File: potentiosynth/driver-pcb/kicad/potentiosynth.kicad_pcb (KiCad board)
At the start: 2 copper layers, 127 x 63.5 mm, 89 parts, among them J1 Conn_01x40, U0 L7815, U1 LM358, U2 LM358, U3 LM358, U4 LM358, U5 LM358, U6 LM358, U7 LM358, U8 LM358

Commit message: first draft driver-pcb
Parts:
- removed QD1, QD2, QD3, QD4, QD5, QD6, QD7, QD8: IRF630, Package_TO_SOT_THT:TO-220-3_Vertical
- removed R0: 10k, Resistor_SMD:R_1206_3216Metric
- removed R1: 68, Resistor_SMD:R_1206_3216Metric
- removed RL1, RL2, RL3, RL4, RL5, RL6, RL7, RL8: 10, Resistor_SMD:R_1206_3216Metric
- removed RV0: 1k, Potentiometer_THT:Potentiometer_Bourns_3296X_Horizontal
- removed TP3: TestPoint, TestPoint:TestPoint_THTPad_D3.0mm_Drill1.5mm
- QE1, QE2, QE3, QE4, QE5, QE6, QE7, QE8: value 2N7000 -> Q_NMOS_GSD; footprint Package_TO_SOT_THT:TO-92_Inline -> Package_TO_SOT_SMD:SOT-23_Handsoldering
- RV1, RV2, RV3, RV4, RV5, RV6, RV7, RV8: value 2k -> R_POT_US
- U0: value L7815 -> R-7815-0.5; footprint Package_TO_SOT_THT:TO-220-3_Vertical -> footprints:CONV_VXO7815-500-M
- U1, U2, U3, U4, U5, U6, U7, U8: value LM358 -> TLV9152IDR; footprint Package_DIP:DIP-8_W7.62mm_LongPads -> Package_SO:SOIC-8_3.9x4.9mm_P1.27mm
- moved TP1 20.3 mm to (158.8, 67.9)
- moved TP2 20.3 mm to (165.1, 67.9)
- moved U2 13.3 mm to (82.5, 99.1)
- moved U3 13.3 mm to (95.2, 99.1)
- moved U4 13.3 mm to (108.0, 99.1)
- moved U5 13.3 mm to (120.7, 99.1)
- moved U6 13.3 mm to (133.3, 99.1)
- moved U7 13.3 mm to (146.1, 99.1)
- moved U8 13.3 mm to (158.8, 99.1)
- moved U1 13.3 mm to (69.8, 99.1)
- moved C3 12.7 mm to (142.2, 71.1)
- moved RF1 10.2 mm to (68.5, 90.2), turned to 180 degrees
- moved RF3 10.1 mm to (93.8, 90.2), turned to 180 degrees
- moved RF2 10.1 mm to (81.2, 90.2), turned to 180 degrees
- moved RF4 10.1 mm to (106.5, 90.2), turned to 180 degrees
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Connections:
- J1 pad 1: /1/RETURN -> /1/REFERENCE
- J1 pad 10: /2/SUPPLY -> /2/COUNTER
- J1 pad 11: /3/RETURN -> /3/REFERENCE
- J1 pad 15: /3/SUPPLY -> /3/COUNTER
- J1 pad 16: /4/RETURN -> /4/REFERENCE
- J1 pad 20: /4/SUPPLY -> /4/COUNTER
- J1 pad 21: /5/RETURN -> /5/REFERENCE
- J1 pad 25: /5/SUPPLY -> /5/COUNTER
- J1 pad 26: /6/RETURN -> /6/REFERENCE
- J1 pad 30: /6/SUPPLY -> /6/COUNTER
- J1 pad 31: /7/RETURN -> /7/REFERENCE
- J1 pad 35: /7/SUPPLY -> /7/COUNTER
- J1 pad 36: /8/RETURN -> /8/REFERENCE
- J1 pad 40: /8/SUPPLY -> /8/COUNTER
- J1 pad 5: /1/SUPPLY -> /1/COUNTER
- J1 pad 6: /2/RETURN -> /2/REFERENCE
- QE1 pad 1: GND -> Net-(QE1-Pad1)
- QE1 pad 2: Net-(QE1-Pad2) -> GND
- QE2 pad 1: GND -> Net-(QE2-Pad1)
- QE2 pad 2: Net-(QE2-Pad2) -> GND
- QE3 pad 1: GND -> Net-(QE3-Pad1)
- QE3 pad 2: Net-(QE3-Pad2) -> GND
- QE4 pad 1: GND -> Net-(QE4-Pad1)
- QE4 pad 2: Net-(QE4-Pad2) -> GND
- QE5 pad 1: GND -> Net-(QE5-Pad1)
- QE5 pad 2: Net-(QE5-Pad2) -> GND
- QE6 pad 1: GND -> Net-(QE6-Pad1)
- QE6 pad 2: Net-(QE6-Pad2) -> GND
- QE7 pad 1: GND -> Net-(QE7-Pad1)
- QE7 pad 2: Net-(QE7-Pad2) -> GND
- QE8 pad 1: GND -> Net-(QE8-Pad1)
- QE8 pad 2: Net-(QE8-Pad2) -> GND
- R+1 pad 1: /1/CONTROL -> Net-(R+1-Pad1)
- R+2 pad 1: /1/CONTROL -> Net-(R+2-Pad1)
- R+3 pad 1: /1/CONTROL -> Net-(R+3-Pad1)
- R+4 pad 1: /1/CONTROL -> Net-(R+4-Pad1)
- R+5 pad 1: /1/CONTROL -> Net-(R+5-Pad1)
- R+6 pad 1: /1/CONTROL -> Net-(R+6-Pad1)
- R+7 pad 1: /1/CONTROL -> Net-(R+7-Pad1)
- R+8 pad 1: /1/CONTROL -> Net-(R+8-Pad1)
- R-1 pad 2: /1/RETURN -> /1/REFERENCE
- R-2 pad 2: /2/RETURN -> /2/REFERENCE
- R-3 pad 2: /3/RETURN -> /3/REFERENCE
- R-4 pad 2: /4/RETURN -> /4/REFERENCE
- R-5 pad 2: /5/RETURN -> /5/REFERENCE
- R-6 pad 2: /6/RETURN -> /6/REFERENCE
- R-7 pad 2: /7/RETURN -> /7/REFERENCE
- R-8 pad 2: /8/RETURN -> /8/REFERENCE
- RF1 pad 2: Net-(QE1-Pad2) -> Net-(QE1-Pad1)
- RF2 pad 2: Net-(QE2-Pad2) -> Net-(QE2-Pad1)
- RF3 pad 2: Net-(QE3-Pad2) -> Net-(QE3-Pad1)
- RF4 pad 2: Net-(QE4-Pad2) -> Net-(QE4-Pad1)
- RF5 pad 2: Net-(QE5-Pad2) -> Net-(QE5-Pad1)
- RF6 pad 2: Net-(QE6-Pad2) -> Net-(QE6-Pad1)
- RF7 pad 2: Net-(QE7-Pad2) -> Net-(QE7-Pad1)
- RF8 pad 2: Net-(QE8-Pad2) -> Net-(QE8-Pad1)
- RV1 pad 1: Net-(RL1-Pad2) -> +15V
- RV1 pad 2: /1/RETURN -> Net-(R+1-Pad1)
- RV1 pad 3: /1/RETURN -> GND
- RV2 pad 1: Net-(RL2-Pad2) -> +15V
- RV2 pad 2: /2/RETURN -> Net-(R+2-Pad1)
- RV2 pad 3: /2/RETURN -> GND
- RV3 pad 1: Net-(RL3-Pad2) -> +15V
- RV3 pad 2: /3/RETURN -> Net-(R+3-Pad1)
- RV3 pad 3: /3/RETURN -> GND
- RV4 pad 1: Net-(RL4-Pad2) -> +15V
- RV4 pad 2: /4/RETURN -> Net-(R+4-Pad1)
- RV4 pad 3: /4/RETURN -> GND
- RV5 pad 1: Net-(RL5-Pad2) -> +15V
- RV5 pad 2: /5/RETURN -> Net-(R+5-Pad1)
- RV5 pad 3: /5/RETURN -> GND
- RV6 pad 1: Net-(RL6-Pad2) -> +15V
- RV6 pad 2: /6/RETURN -> Net-(R+6-Pad1)
- RV6 pad 3: /6/RETURN -> GND
- RV7 pad 1: Net-(RL7-Pad2) -> +15V
- RV7 pad 2: /7/RETURN -> Net-(R+7-Pad1)
- RV7 pad 3: /7/RETURN -> GND
- RV8 pad 1: Net-(RL8-Pad2) -> +15V
- RV8 pad 2: /8/RETURN -> Net-(R+8-Pad1)
- RV8 pad 3: /8/RETURN -> GND
- U1 pad 1: Net-(QE1-Pad2) -> Net-(QE1-Pad1)
- U1 pad 5: /1/CONTROL -> Net-(R+1-Pad1)
- U1 pad 6: /1/RETURN -> /1/REFERENCE
- U1 pad 7: Net-(QD1-Pad1) -> /1/COUNTER
- U2 pad 1: Net-(QE2-Pad2) -> Net-(QE2-Pad1)
- U2 pad 5: /1/CONTROL -> Net-(R+2-Pad1)
- U2 pad 6: /2/RETURN -> /2/REFERENCE
- U2 pad 7: Net-(QD2-Pad1) -> /2/COUNTER
- U3 pad 1: Net-(QE3-Pad2) -> Net-(QE3-Pad1)
- U3 pad 5: /1/CONTROL -> Net-(R+3-Pad1)
- U3 pad 6: /3/RETURN -> /3/REFERENCE
- U3 pad 7: Net-(QD3-Pad1) -> /3/COUNTER
- U4 pad 1: Net-(QE4-Pad2) -> Net-(QE4-Pad1)
- U4 pad 5: /1/CONTROL -> Net-(R+4-Pad1)
- U4 pad 6: /4/RETURN -> /4/REFERENCE
- U4 pad 7: Net-(QD4-Pad1) -> /4/COUNTER
- U5 pad 1: Net-(QE5-Pad2) -> Net-(QE5-Pad1)
- U5 pad 5: /1/CONTROL -> Net-(R+5-Pad1)
- U5 pad 6: /5/RETURN -> /5/REFERENCE
- U5 pad 7: Net-(QD5-Pad1) -> /5/COUNTER
- U6 pad 1: Net-(QE6-Pad2) -> Net-(QE6-Pad1)
- U6 pad 5: /1/CONTROL -> Net-(R+6-Pad1)
- U6 pad 6: /6/RETURN -> /6/REFERENCE
- U6 pad 7: Net-(QD6-Pad1) -> /6/COUNTER
- U7 pad 1: Net-(QE7-Pad2) -> Net-(QE7-Pad1)
- U7 pad 5: /1/CONTROL -> Net-(R+7-Pad1)
- U7 pad 6: /7/RETURN -> /7/REFERENCE
- U7 pad 7: Net-(QD7-Pad1) -> /7/COUNTER
- U8 pad 1: Net-(QE8-Pad2) -> Net-(QE8-Pad1)
- U8 pad 5: /1/CONTROL -> Net-(R+8-Pad1)
- U8 pad 6: /8/RETURN -> /8/REFERENCE
- U8 pad 7: Net-(QD8-Pad1) -> /8/COUNTER
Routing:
- net +15V: track 556.7 -> 209.4 mm, vias 1 -> 8
- net /1/CONTROL: track 283.7 -> 0.00 mm, vias 16 -> 0
- net /2/REFERENCE: track 0.00 -> 40.2 mm
- net /8/REFERENCE: track 0.00 -> 39.9 mm
- net /4/REFERENCE: track 0.00 -> 39.9 mm
- net /3/REFERENCE: track 0.00 -> 39.9 mm
- net /5/REFERENCE: track 0.00 -> 39.9 mm
- net /7/REFERENCE: track 0.00 -> 39.7 mm
- net /1/REFERENCE: track 0.00 -> 39.7 mm
- net /6/REFERENCE: track 0.00 -> 39.7 mm
- net /7/RETURN: track 39.2 -> 0.00 mm, vias 1 -> 0
- net /6/RETURN: track 39.2 -> 0.00 mm, vias 1 -> 0
- net /5/RETURN: track 39.2 -> 0.00 mm, vias 1 -> 0
- net /4/RETURN: track 38.4 -> 0.00 mm, vias 1 -> 0
- net /3/RETURN: track 38.4 -> 0.00 mm, vias 1 -> 0
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- added copper zone on B.Cu, net +15V
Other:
- net class Default: clearance 0.2 -> 0.127
- rule trace_clearance: 0.2 -> 0.127
- board text added: "18 to 30 V"
- board text added: "BLAISE THOMPSON UW-MADISON DEPARTMENT OF CHEMISTRY WICKENS GROUP"
- board text added: "POTENTIOSYNTH REVISION A MAY 2021"
- board text removed: "BLAISE THOMPSON UW-MADISON DEPARTMENT OF CHEMISTRY INSTRUMENT SHOP"
- board text removed: "REVISION 4.1.1 MARCH 2020"
- board text removed: "≥ 18 V CENTER POSITIVE"

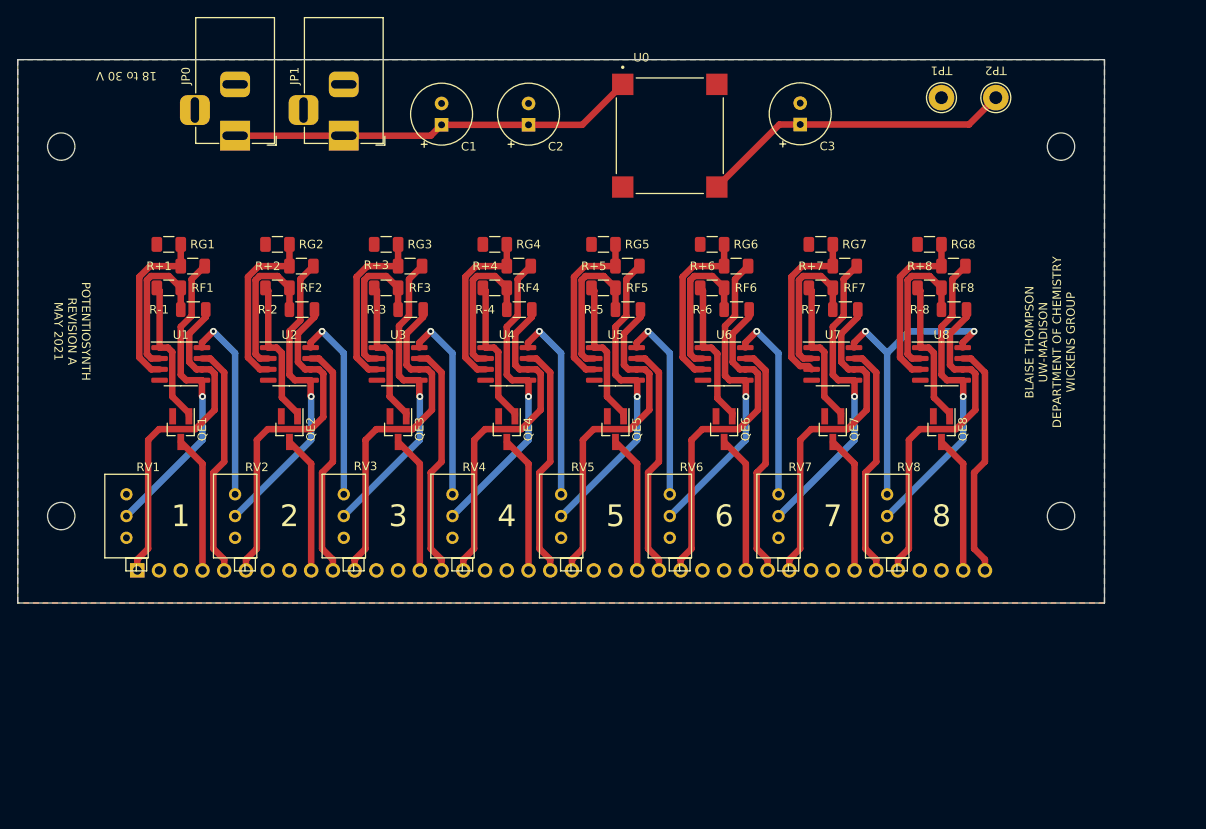
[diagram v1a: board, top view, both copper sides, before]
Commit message: added buffer amplifier
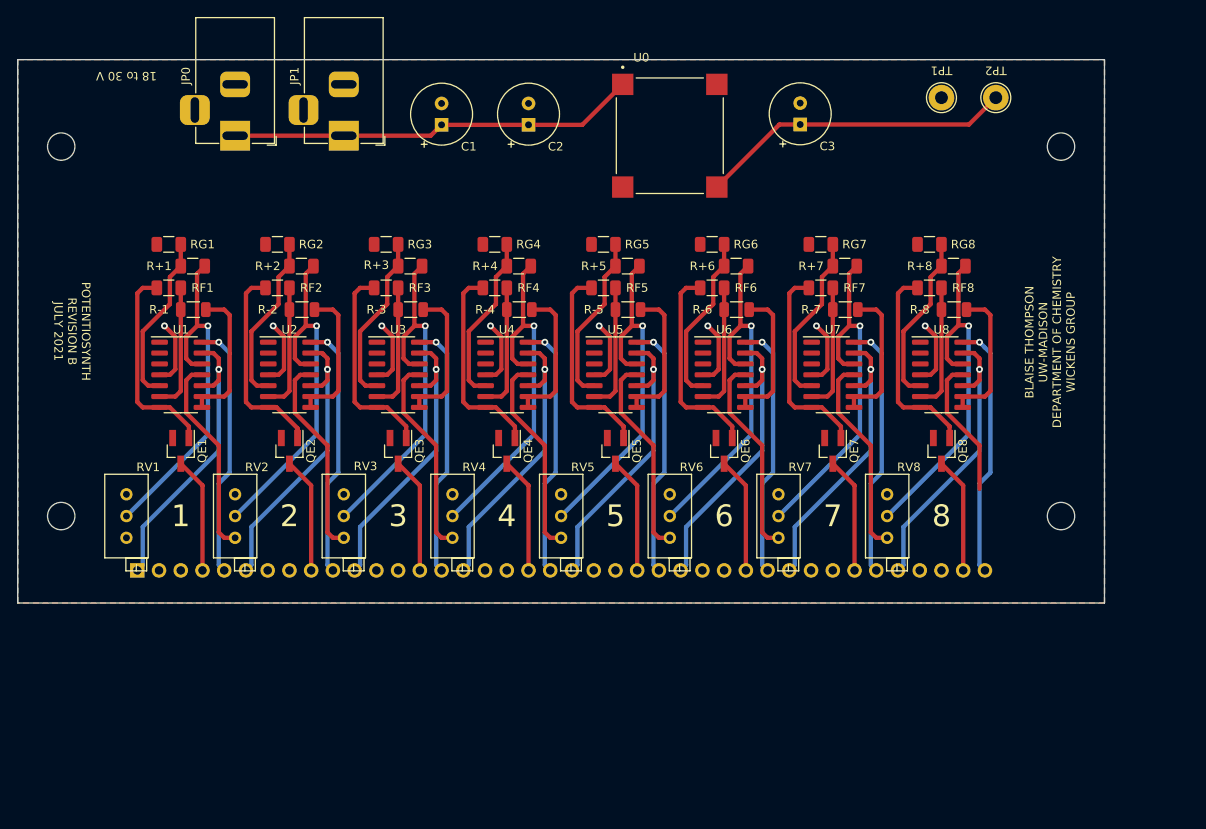
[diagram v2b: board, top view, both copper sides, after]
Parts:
- QE1, QE2, QE3, QE4, QE5, QE6, QE7, QE8: value Q_NMOS_GSD -> 2N70002K
- U1, U2, U3, U4, U5, U6, U7, U8: value TLV9152IDR -> TLV9154IDR; footprint Package_SO:SOIC-8_3.9x4.9mm_P1.27mm -> Package_SO:SOIC-14_3.9x8.7mm_P1.27mm
- moved QE1 2.54 mm to (69.8, 109.2)
- moved QE2 2.54 mm to (82.5, 109.2)
- moved QE3 2.54 mm to (95.2, 109.2)
- moved QE4 2.54 mm to (108.0, 109.2)
- moved QE5 2.54 mm to (120.7, 109.2)
- moved QE6 2.54 mm to (133.3, 109.2)
- moved QE7 2.54 mm to (146.1, 109.2)
- moved QE8 2.54 mm to (158.8, 109.2)
- moved U1 1.27 mm to (69.8, 100.3)
- moved U2 1.27 mm to (82.5, 100.3)
- moved U3 1.27 mm to (95.2, 100.3)
- moved U4 1.27 mm to (108.0, 100.3)
- moved U5 1.27 mm to (120.7, 100.3)
- moved U6 1.27 mm to (133.3, 100.3)
- moved U7 1.27 mm to (146.1, 100.3)
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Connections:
- R-1 pad 2: /1/REFERENCE -> Net-(R-1-Pad2)
- R-2 pad 2: /2/REFERENCE -> Net-(R-2-Pad2)
- R-3 pad 2: /3/REFERENCE -> Net-(R-3-Pad2)
- R-4 pad 2: /4/REFERENCE -> Net-(R-4-Pad2)
- R-5 pad 2: /5/REFERENCE -> Net-(R-5-Pad2)
- R-6 pad 2: /6/REFERENCE -> Net-(R-6-Pad2)
- R-7 pad 2: /7/REFERENCE -> Net-(R-7-Pad2)
- R-8 pad 2: /8/REFERENCE -> Net-(R-8-Pad2)
- U1 pad 1: Net-(QE1-Pad1) -> (no net)
- U1 pad 2: Net-(R-1-Pad1) -> (no net)
- U1 pad 3: Net-(R+1-Pad2) -> (no net)
- U1 pad 4: GND -> +15V
- U1 pad 5: Net-(R+1-Pad1) -> Net-(R+1-Pad2)
- U1 pad 6: /1/REFERENCE -> Net-(R-1-Pad1)
- U1 pad 7: /1/COUNTER -> Net-(QE1-Pad1)
- U1 pad 8: +15V -> Net-(R-1-Pad2)
- U2 pad 1: Net-(QE2-Pad1) -> (no net)
- U2 pad 2: Net-(R-2-Pad1) -> (no net)
- U2 pad 3: Net-(R+2-Pad2) -> (no net)
- U2 pad 4: GND -> +15V
- U2 pad 5: Net-(R+2-Pad1) -> Net-(R+2-Pad2)
- U2 pad 6: /2/REFERENCE -> Net-(R-2-Pad1)
- U2 pad 7: /2/COUNTER -> Net-(QE2-Pad1)
- U2 pad 8: +15V -> Net-(R-2-Pad2)
- U3 pad 1: Net-(QE3-Pad1) -> (no net)
- U3 pad 2: Net-(R-3-Pad1) -> (no net)
- U3 pad 3: Net-(R+3-Pad2) -> (no net)
- U3 pad 4: GND -> +15V
- U3 pad 5: Net-(R+3-Pad1) -> Net-(R+3-Pad2)
- U3 pad 6: /3/REFERENCE -> Net-(R-3-Pad1)
- U3 pad 7: /3/COUNTER -> Net-(QE3-Pad1)
- U3 pad 8: +15V -> Net-(R-3-Pad2)
- U4 pad 1: Net-(QE4-Pad1) -> (no net)
- U4 pad 2: Net-(R-4-Pad1) -> (no net)
- U4 pad 3: Net-(R+4-Pad2) -> (no net)
- U4 pad 4: GND -> +15V
- U4 pad 5: Net-(R+4-Pad1) -> Net-(R+4-Pad2)
- U4 pad 6: /4/REFERENCE -> Net-(R-4-Pad1)
- U4 pad 7: /4/COUNTER -> Net-(QE4-Pad1)
- U4 pad 8: +15V -> Net-(R-4-Pad2)
- U5 pad 1: Net-(QE5-Pad1) -> (no net)
- U5 pad 2: Net-(R-5-Pad1) -> (no net)
- U5 pad 3: Net-(R+5-Pad2) -> (no net)
- U5 pad 4: GND -> +15V
- U5 pad 5: Net-(R+5-Pad1) -> Net-(R+5-Pad2)
- U5 pad 6: /5/REFERENCE -> Net-(R-5-Pad1)
- U5 pad 7: /5/COUNTER -> Net-(QE5-Pad1)
- U5 pad 8: +15V -> Net-(R-5-Pad2)
- U6 pad 1: Net-(QE6-Pad1) -> (no net)
- U6 pad 2: Net-(R-6-Pad1) -> (no net)
- U6 pad 3: Net-(R+6-Pad2) -> (no net)
- U6 pad 4: GND -> +15V
- U6 pad 5: Net-(R+6-Pad1) -> Net-(R+6-Pad2)
- U6 pad 6: /6/REFERENCE -> Net-(R-6-Pad1)
- U6 pad 7: /6/COUNTER -> Net-(QE6-Pad1)
- U6 pad 8: +15V -> Net-(R-6-Pad2)
- U7 pad 1: Net-(QE7-Pad1) -> (no net)
- U7 pad 2: Net-(R-7-Pad1) -> (no net)
- U7 pad 3: Net-(R+7-Pad2) -> (no net)
- U7 pad 4: GND -> +15V
- U7 pad 5: Net-(R+7-Pad1) -> Net-(R+7-Pad2)
- U7 pad 6: /7/REFERENCE -> Net-(R-7-Pad1)
- U7 pad 7: /7/COUNTER -> Net-(QE7-Pad1)
- U7 pad 8: +15V -> Net-(R-7-Pad2)
- U8 pad 1: Net-(QE8-Pad1) -> (no net)
- U8 pad 2: Net-(R-8-Pad1) -> (no net)
- U8 pad 3: Net-(R+8-Pad2) -> (no net)
- U8 pad 4: GND -> +15V
- U8 pad 5: Net-(R+8-Pad1) -> Net-(R+8-Pad2)
- U8 pad 6: /8/REFERENCE -> Net-(R-8-Pad1)
- U8 pad 7: /8/COUNTER -> Net-(QE8-Pad1)
- U8 pad 8: +15V -> Net-(R-8-Pad2)
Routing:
- net GND: track 0.00 -> 181.8 mm
- net +15V: track 209.4 -> 99.4 mm
- net Net-(R-3-Pad2): track 0.00 -> 16.7 mm
- net Net-(R-4-Pad2): track 0.00 -> 16.7 mm
- net Net-(R-8-Pad2): track 0.00 -> 16.7 mm
- net Net-(R-6-Pad2): track 0.00 -> 16.7 mm
- net Net-(R-2-Pad2): track 0.00 -> 16.7 mm
- net Net-(R-5-Pad2): track 0.00 -> 16.7 mm
- net Net-(R-1-Pad2): track 0.00 -> 16.7 mm
- net Net-(R-7-Pad2): track 0.00 -> 16.7 mm
- net Net-(QE1-Pad1): track 17.1 -> 24.3 mm
- net Net-(QE4-Pad1): track 17.1 -> 23.8 mm
- net Net-(QE7-Pad1): track 17.1 -> 23.8 mm
- net Net-(QE5-Pad1): track 17.1 -> 23.8 mm
- net Net-(QE6-Pad1): track 17.1 -> 23.8 mm
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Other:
- net class Default: trace_width 0.762 -> 0.508
- board text added: "POTENTIOSYNTH REVISION B JULY 2021"
- board text removed: "POTENTIOSYNTH REVISION A MAY 2021"

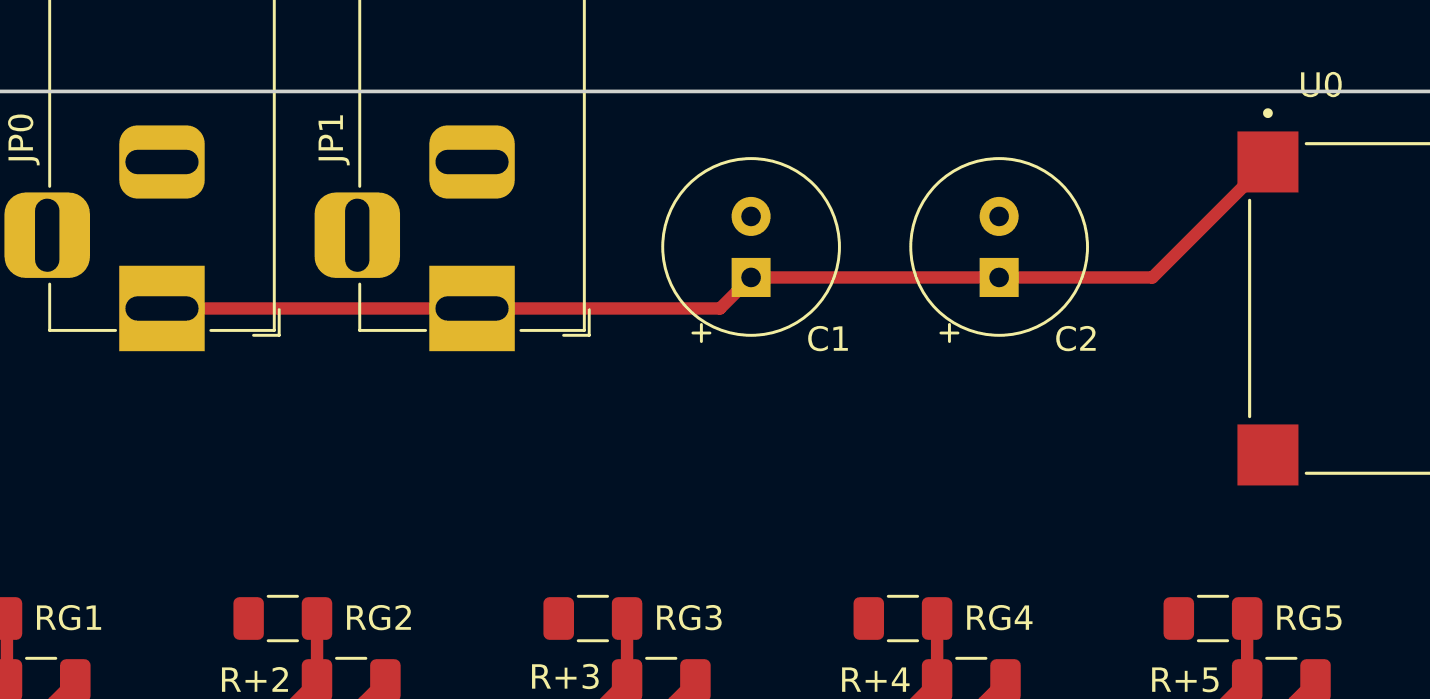
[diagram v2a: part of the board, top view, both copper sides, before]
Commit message: add fuse
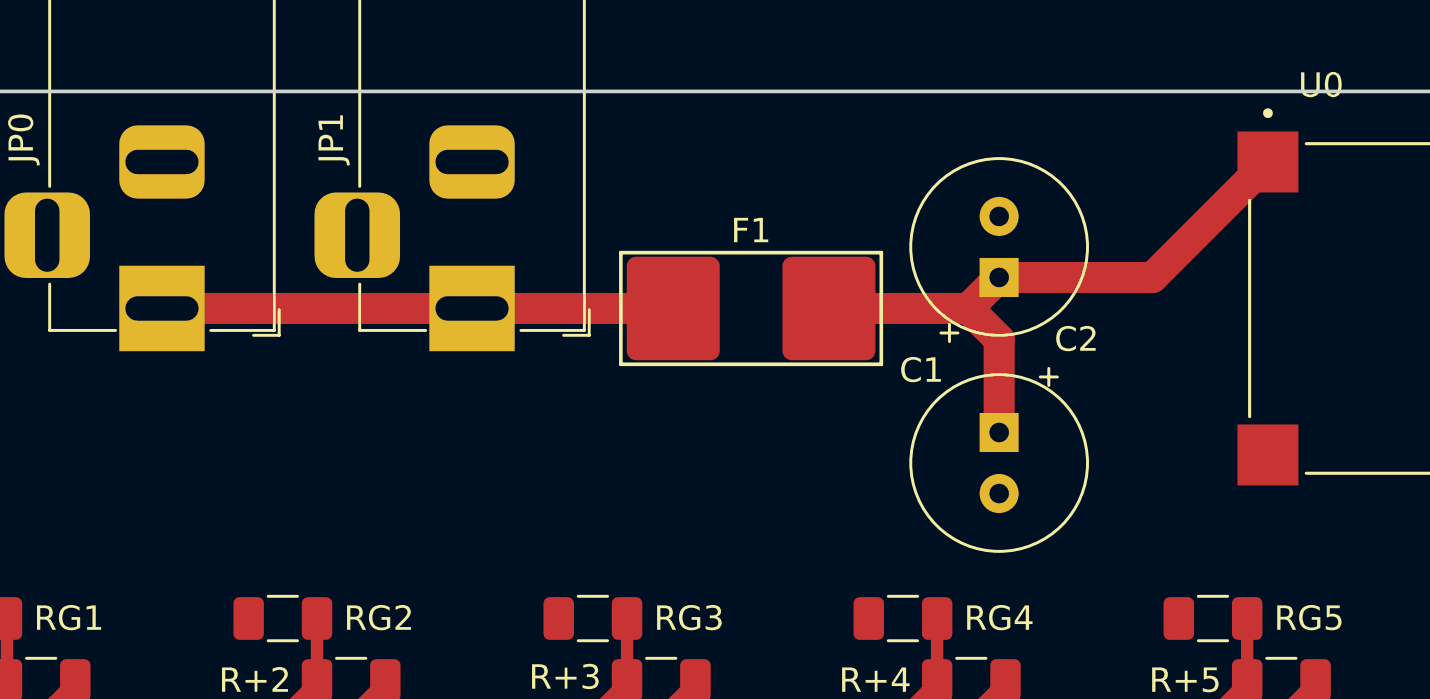
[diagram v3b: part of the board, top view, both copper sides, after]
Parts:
- added F1: Fuse, footprints:01550900M, F.Cu at (100.3, 72.4)
- moved C1 12.0 mm to (110.5, 77.5), turned to 270 degrees
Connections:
- JP0 pad 1: Net-(C1-Pad1) -> Net-(F1-Pad1)
- JP1 pad 1: Net-(C1-Pad1) -> Net-(F1-Pad1)
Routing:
- net Net-(C1-Pad1): track 47.8 -> 26.1 mm
- net Net-(F1-Pad1): track 0.00 -> 20.9 mm
